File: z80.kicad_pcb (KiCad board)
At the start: 2 copper layers, 119.4 x 121.9 mm, 70 parts, among them SW1 RESET, SW2 STEP, U1 Z80CPU, U2 74HC04, U3 74AC541, U4 74LS138, U5 74HC245, U6 74LS148, Y1 7.3728MHz

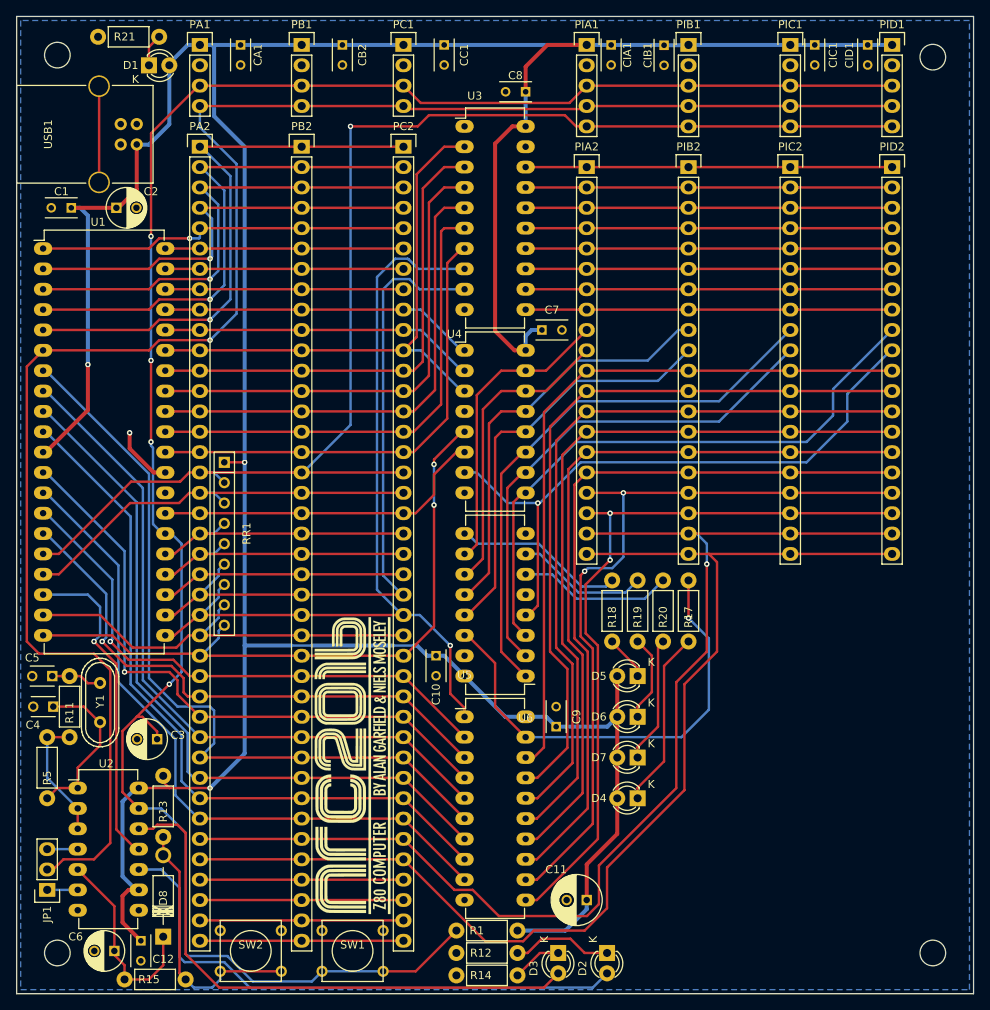
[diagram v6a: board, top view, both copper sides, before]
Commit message: New layout complete. Now with rc2014 compat. slots!
Plus on board address decoding, single stepping using M1 line so button
is click per instruction. Board is also much smaller!
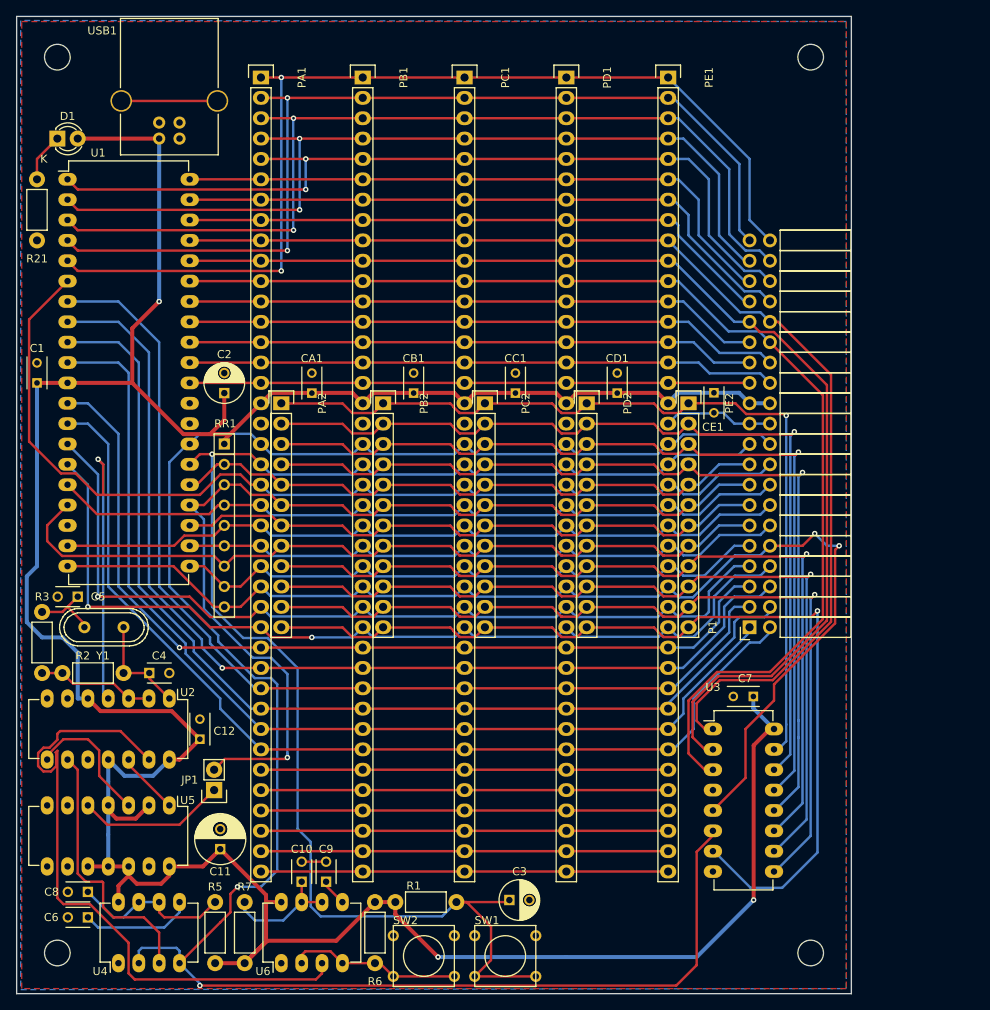
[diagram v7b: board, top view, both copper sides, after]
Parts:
- removed CB2, CIA1, CIB1, CIC1, CID1: 100n, Capacitors_ThroughHole:C_Rect_L4_W2.5_P2.5
- removed D2, D3, D4, D5, D6, D7: LED, LEDs:LED-3MM
- removed D8: D, Diodes_ThroughHole:Diode_DO-41_SOD81_Horizontal_RM10
- removed the G*** at (82.7, 124.0)
- removed PIA1, PIB1, PIC1, PID1: CONN_01X05, Socket_Strips:Socket_Strip_Straight_1x05
- removed PIA2, PIB2, PIC2, PID2: CONN_01X20, Socket_Strips:Socket_Strip_Straight_1x20
- removed R11: 1K, Resistors_ThroughHole:Resistor_Horizontal_RM7mm
- removed R12, R14, R17, R18, R19, R20: 220, Resistors_ThroughHole:Resistor_Horizontal_RM7mm
- removed R13: 82K, Resistors_ThroughHole:Resistor_Horizontal_RM7mm
- removed R15: 18K, Resistors_ThroughHole:Resistor_Horizontal_RM7mm
- added CB1: 100n, Capacitors_ThroughHole:C_Rect_L4_W2.5_P2.5, F.Cu at (90.2, 77.5)
- added CD1: 100n, Capacitors_ThroughHole:C_Rect_L4_W2.5_P2.5, F.Cu at (115.6, 77.5)
- added CE1: 100n, Capacitors_ThroughHole:C_Rect_L4_W2.5_P2.5, F.Cu at (127.6, 77.4)
- added G***: LOGO, ncr2016_logo:nrc2016_logo_1200, B.Cu at (54.6, 75.6)
- added P1: CONN_02X20, Socket_Strips:Socket_Strip_Angled_2x20, F.Cu at (132.1, 106.7)
- added PD1: CONN_01X40, Socket_Strips:Socket_Strip_Straight_1x40, F.Cu at (109.2, 38.1)
- added PD2: CONN_01X12, Socket_Strips:Socket_Strip_Straight_1x12, F.Cu at (111.8, 78.7)
- added PE1: CONN_01X40, Socket_Strips:Socket_Strip_Straight_1x40, F.Cu at (121.9, 38.1)
- added PE2: CONN_01X12, Socket_Strips:Socket_Strip_Straight_1x12, F.Cu at (124.5, 78.7)
- added R2: 1M, Resistors_ThroughHole:Resistor_Horizontal_RM7mm, F.Cu at (46.4, 112.4)
- added R3: 1K, Resistors_ThroughHole:Resistor_Horizontal_RM7mm, F.Cu at (43.8, 112.4)
- added R6: 10K, Resistors_ThroughHole:Resistor_Horizontal_RM7mm, F.Cu at (85.3, 141.0)
- added R7: 1K, Resistors_ThroughHole:Resistor_Horizontal_RM7mm, F.Cu at (69.1, 148.6)
- C1, C12: value 100nF -> 100n
- C10, C8, C9: value 100n -> 10n; footprint Capacitors_ThroughHole:C_Rect_L4_W2.5_P2.5 -> Capacitors_ThroughHole:C_Disc_D3_P2.5
- C6: value 1uF -> 10n; footprint Capacitors_ThroughHole:C_Radial_D5_L11_P2.5 -> Capacitors_ThroughHole:C_Disc_D3_P2.5
- JP1: value JUMPER3 -> JUMPER; footprint Pin_Headers:Pin_Header_Straight_1x03 -> Pin_Headers:Pin_Header_Straight_1x02
- PA1, PB1, PC1: value CONN_01X04 -> CONN_01X40; footprint Socket_Strips:Socket_Strip_Straight_1x04 -> Socket_Strips:Socket_Strip_Straight_1x40
- PA2, PB2, PC2: value CONN_01X40 -> CONN_01X12; footprint Socket_Strips:Socket_Strip_Straight_1x40 -> Socket_Strips:Socket_Strip_Straight_1x12
- R5: value 1M -> 1K
- U3: value 74AC541 -> 74LS138; footprint Housings_DIP:DIP-20_W7.62mm_LongPads -> Housings_DIP:DIP-16_W7.62mm_LongPads
- U4: value 74LS138 -> LM555N; footprint Housings_DIP:DIP-16_W7.62mm_LongPads -> Housings_DIP:DIP-8_W7.62mm_LongPads
- U5: value 74HC245 -> 74HC74; footprint Housings_DIP:DIP-20_W7.62mm_LongPads -> Housings_DIP:DIP-14_W7.62mm_LongPads
- U6: value 74LS148 -> LM555N; footprint Housings_DIP:DIP-16_W7.62mm_LongPads -> Housings_DIP:DIP-8_W7.62mm_LongPads
- moved C8 113.8 mm to (49.5, 139.7)
- moved U4 87.8 mm to (53.3, 148.6), turned to 90 degrees
- moved U3 81.3 mm to (127.5, 119.4)
- moved C7 52.8 mm to (132.5, 115.3), turned to 180 degrees
- moved C3 48.3 mm to (102.1, 140.7), turned to 0 degrees
- moved U6 47.0 mm to (73.7, 148.6), turned to 90 degrees
- moved C11 46.2 mm to (66.0, 134.4), turned to 90 degrees
- moved CA1 44.3 mm to (77.5, 77.5), turned to 90 degrees
- moved CC1 44.3 mm to (102.9, 77.5), turned to 90 degrees
- moved U5 38.5 mm to (59.7, 128.9), turned to 270 degrees
- moved R5 35.1 mm to (65.4, 148.6), turned to 90 degrees
- moved C9 34.6 mm to (79.2, 138.4)
- moved PA2 33.6 mm to (73.7, 78.7)
- moved PB2 33.6 mm to (86.4, 78.7)
- moved PC2 33.6 mm to (99.1, 78.7)
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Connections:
- C10 pad 1: VCC -> Net-(C10-Pad1)
- C8 pad 1: VCC -> Net-(C8-Pad1)
- C9 pad 1: VCC -> Net-(C9-Pad1)
- JP1 pad 2: /~CLK -> /~WAIT
- PA1 pad 1: VCC -> /A15
- PA1 pad 2: GND -> /A14
- PA1 pad 3: /~RESET -> /A13
- PA1 pad 4: /~CLK -> /A12
- PA2 pad 1: /A15 -> /Card Slots/~IOSEL1
- PA2 pad 10: /A6 -> /Card Slots/~IOSEL6
- PA2 pad 11: /A5 -> /Card Slots/~IOSEL7
- PA2 pad 12: /A4 -> /Card Slots/~IOSEL8
- PA2 pad 2: /A14 -> /Card Slots/~IOSEL2
- PA2 pad 3: /A13 -> /Card Slots/~IOSEL3
- PA2 pad 4: /A12 -> /Card Slots/~IOSEL4
- PA2 pad 5: /A11 -> /~BUSRQ
- PA2 pad 6: /A10 -> /~WAIT
- PA2 pad 7: /A9 -> /~BUSACK
- PA2 pad 8: /A8 -> /~NMI
- PA2 pad 9: /A7 -> /Card Slots/~IOSEL5
- PB1 pad 1: VCC -> /A15
- PB1 pad 2: GND -> /A14
- PB1 pad 3: /~RESET -> /A13
- PB1 pad 4: /~CLK -> /A12
- PB2 pad 1: /A15 -> /Card Slots/~IOSEL1
- PB2 pad 10: /A6 -> /Card Slots/~IOSEL6
- PB2 pad 11: /A5 -> /Card Slots/~IOSEL7
- PB2 pad 12: /A4 -> /Card Slots/~IOSEL8
- PB2 pad 2: /A14 -> /Card Slots/~IOSEL2
- PB2 pad 3: /A13 -> /Card Slots/~IOSEL3
- PB2 pad 4: /A12 -> /Card Slots/~IOSEL4
- PB2 pad 5: /A11 -> /~BUSRQ
- PB2 pad 6: /A10 -> /~WAIT
- PB2 pad 7: /A9 -> /~BUSACK
- PB2 pad 8: /A8 -> /~NMI
- PB2 pad 9: /A7 -> /Card Slots/~IOSEL5
- PC1 pad 1: VCC -> /A15
- PC1 pad 2: GND -> /A14
- PC1 pad 3: /~RESET -> /A13
- PC1 pad 4: /~CLK -> /A12
- PC2 pad 1: /A15 -> /Card Slots/~IOSEL1
- PC2 pad 10: /A6 -> /Card Slots/~IOSEL6
- PC2 pad 11: /A5 -> /Card Slots/~IOSEL7
- PC2 pad 12: /A4 -> /Card Slots/~IOSEL8
- PC2 pad 2: /A14 -> /Card Slots/~IOSEL2
- PC2 pad 3: /A13 -> /Card Slots/~IOSEL3
- PC2 pad 4: /A12 -> /Card Slots/~IOSEL4
- PC2 pad 5: /A11 -> /~BUSRQ
- PC2 pad 6: /A10 -> /~WAIT
- PC2 pad 7: /A9 -> /~BUSACK
- PC2 pad 8: /A8 -> /~NMI
- PC2 pad 9: /A7 -> /Card Slots/~IOSEL5
- R5 pad 1: Net-(R11-Pad1) -> VCC
- R5 pad 2: Net-(C4-Pad1) -> Net-(C8-Pad1)
- RR1 pad 2: /~INT -> /~BUSRQ
- RR1 pad 3: /~NMI -> /~WAIT
- RR1 pad 4: /~BUSRQ -> /~INT
- RR1 pad 5: /~WAIT -> /~MREQ
- RR1 pad 7: /~RD -> /~NMI
- RR1 pad 8: /~MREQ -> /~RD
- SW2 pad 2: Net-(D8-Pad2) -> Net-(R6-Pad2)
- U1 pad 18: /CPU/~HALT -> (no net)
- U2 pad 10: Net-(D2-Pad2) -> (no net)
- U2 pad 11: /CPU/~HALT -> VCC
- U2 pad 12: Net-(D3-Pad2) -> Net-(U2-Pad12)
- U2 pad 13: /~RESET -> Net-(U2-Pad13)
- U2 pad 2: Net-(R11-Pad1) -> Net-(R2-Pad1)
- U2 pad 3: Net-(R11-Pad1) -> Net-(R2-Pad1)
- U2 pad 4: Net-(JP1-Pad3) -> /~CLK
- U2 pad 5: Net-(C6-Pad1) -> VCC
- U2 pad 6: Net-(JP1-Pad1) -> (no net)
- U2 pad 8: (no net) -> Net-(U2-Pad8)
- U2 pad 9: VCC -> Net-(U2-Pad9)
- U3 pad 1: GND -> /A7
- U3 pad 10: GND -> /Card Slots/~IOSEL6
- U3 pad 11: /IO/~WR-B -> /Card Slots/~IOSEL5
- U3 pad 12: /IO/~RD-B -> /Card Slots/~IOSEL4
- U3 pad 13: /IO/A0-B -> /Card Slots/~IOSEL3
- U3 pad 14: /IO/A1-B -> /Card Slots/~IOSEL2
- U3 pad 15: /IO/A2-B -> /Card Slots/~IOSEL1
- U3 pad 16: /IO/A3-B -> VCC
- U3 pad 2: /A5 -> /A6
- U3 pad 3: /A4 -> /A5
- U3 pad 4: /A3 -> GND
- U3 pad 5: /A2 -> /~IORQ
- U3 pad 6: /A1 -> /~M1
- U3 pad 7: /A0 -> /Card Slots/~IOSEL8
- U3 pad 8: /~RD -> GND
- U3 pad 9: /~WR -> /Card Slots/~IOSEL7
- U4 pad 1: /A7 -> GND
- U4 pad 2: /A6 -> /~M1
- U4 pad 3: /A5 -> Net-(U2-Pad9)
- U4 pad 4: GND -> /~M1
- U4 pad 5: /~IORQ -> Net-(C6-Pad1)
- U4 pad 6: /~M1 -> Net-(C8-Pad1)
- U4 pad 7: /IO/~IOSEL8 -> Net-(C8-Pad1)
- U4 pad 8: GND -> VCC
- U5 pad 1: /~RD -> Net-(U2-Pad12)
- U5 pad 10: GND -> VCC
- U5 pad 11: /IO/D7-B -> VCC
- U5 pad 12: /IO/D6-B -> VCC
- U5 pad 13: /IO/D5-B -> (no net)
- U5 pad 14: /IO/D4-B -> VCC
- U5 pad 2: /D0 -> VCC
- U5 pad 3: /D1 -> Net-(U2-Pad8)
- U5 pad 4: /D2 -> VCC
- U5 pad 5: /D3 -> Net-(JP1-Pad1)
- U5 pad 6: /D4 -> (no net)
- U5 pad 7: /D5 -> GND
- U5 pad 8: /D6 -> (no net)
- U5 pad 9: /D7 -> (no net)
- U6 pad 1: /IO/~IOSEL5 -> GND
- U6 pad 2: /IO/~IOSEL6 -> Net-(R6-Pad2)
- U6 pad 3: /IO/~IOSEL7 -> Net-(U2-Pad13)
- U6 pad 4: /IO/~IOSEL8 -> Net-(R6-Pad2)
- U6 pad 5: GND -> Net-(C9-Pad1)
- U6 pad 6: /IO/S-LED2 -> Net-(C10-Pad1)
- U6 pad 7: /IO/S-LED1 -> Net-(C10-Pad1)
- U6 pad 8: GND -> VCC
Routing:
- net /~M1: track 42.1 -> 251.1 mm, vias 0 -> 2
- net /S1: track 145.8 -> 0.00 mm, vias 1 -> 0
- net /S2: track 145.1 -> 0.00 mm
- net /Card Slots/~IOSEL8: track 0.00 -> 118.5 mm, vias 0 -> 1
- net /Card Slots/~IOSEL4: track 0.00 -> 113.3 mm, vias 0 -> 1
- net /Card Slots/~IOSEL3: track 0.00 -> 112.6 mm, vias 0 -> 1
- net /Card Slots/~IOSEL2: track 0.00 -> 111.9 mm, vias 0 -> 1
- net /Card Slots/~IOSEL1: track 0.00 -> 110.1 mm, vias 0 -> 1
- net /Card Slots/~IOSEL7: track 0.00 -> 107.8 mm, vias 0 -> 1
- net /Card Slots/~IOSEL6: track 0.00 -> 107.1 mm, vias 0 -> 1
- net /Card Slots/~IOSEL5: track 0.00 -> 106.4 mm, vias 0 -> 1
- net /A6: track 39.4 -> 143.8 mm
- net /A7: track 39.4 -> 143.4 mm
- net /IO/D6-B: track 95.8 -> 0.00 mm, vias 2 -> 0
- net /IO/D7-B: track 93.2 -> 0.00 mm, vias 2 -> 0
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- added copper zone on F.Cu, net GND
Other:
- board size 119.4 x 121.9 mm -> 104.1 x 121.9 mm
